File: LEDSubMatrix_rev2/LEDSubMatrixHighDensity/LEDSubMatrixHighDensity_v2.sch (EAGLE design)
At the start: 145 parts, among them IC1 TLC5955DCAR, IC2 TLC5955DCAR, IC3 TLC5955DCAR, IC4 TLC5955DCAR, IC5 TLC5955DCAR, IC6 TLC5955DCAR, IC7 TLC5955DCAR, IC8 TLC5955DCAR

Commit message: Updated pinouts to align with control board
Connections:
- new net 3V3_LOGIC: C1.1, C1B.1, C2.1, C2B.1, C3.1, C3B.1, C4.1, C4B.1, C5.1, C5B.1, C6.1, C6B.1, C7.1, C7B.1, C8.1, C8B.1, IC1.VCC, IC2.VCC, IC3.VCC, IC4.VCC, IC5.VCC, IC6.VCC, IC7.VCC, IC8.VCC, SV1.1
- net 3V3: no longer C1.1, C1B.1, C2.1, C2B.1, C3.1, C3B.1, C4.1, C4B.1, C5.1, C5B.1, C6.1, C6B.1, C7.1, C7B.1, C8.1, C8B.1, IC1.VCC, IC2.VCC, IC3.VCC, IC4.VCC, IC5.VCC, IC6.VCC, IC7.VCC, IC8.VCC
- net GND: now also SV1.2, SV1.4; no longer SV1.10, SV1.12, SV1.9
- net GSCLK: now also SV1.3; no longer SV1.11
- net SCLK: now also SV1.7; no longer SV1.1
- net SIN_1,2: now also SV1.12; no longer SV1.2
- net SIN_3,4: now also SV1.11; no longer SV1.3
- net SIN_5,6: now also SV1.10; no longer SV1.4
- net SIN_7,8: now also SV1.9; no longer SV1.7

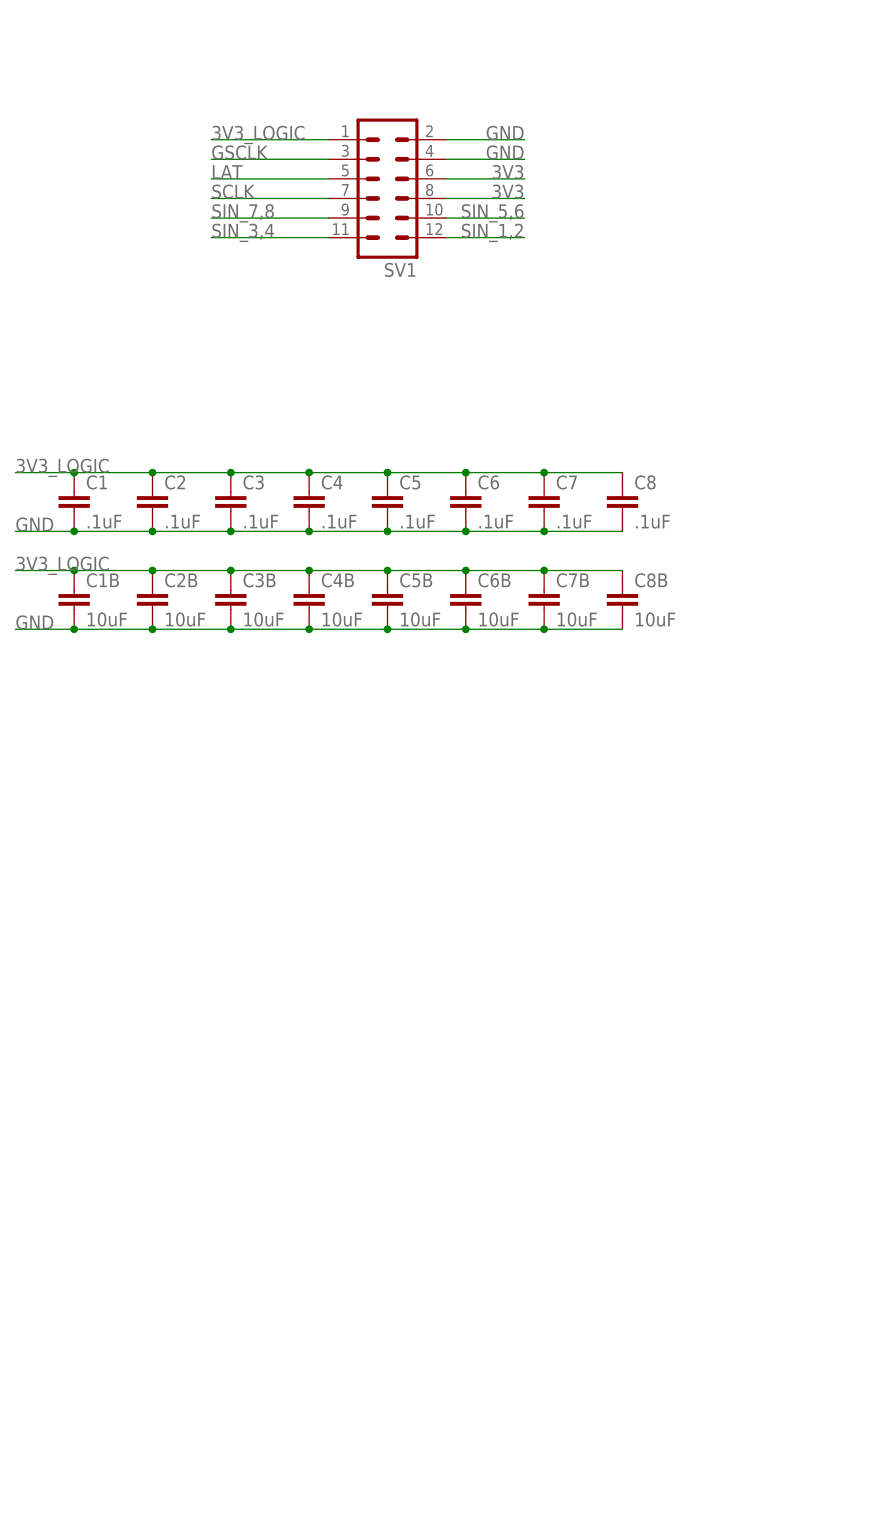
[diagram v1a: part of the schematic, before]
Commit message: Added logic buffers to LED matrix
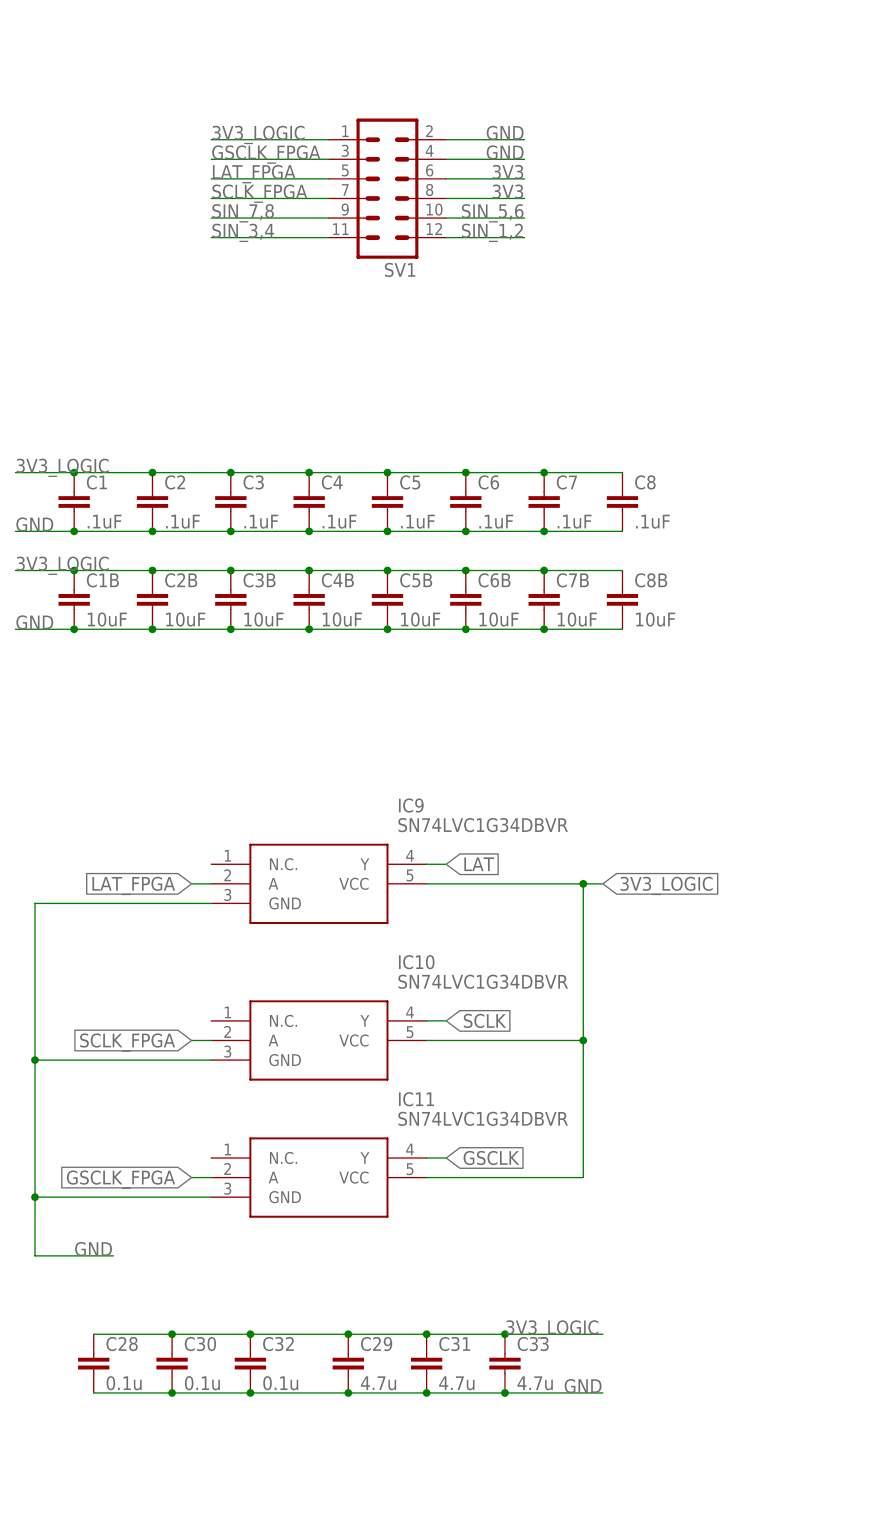
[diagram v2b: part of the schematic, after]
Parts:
- added C28, C30, C32: 0.1u, GTOR - Passive Components:CAP_SMDC0603
- added C29, C31, C33: 4.7u, GTOR - Passive Components:CAP_SMDC0603
- added IC10, IC11, IC9: SN74LVC1G34DBVR, SN74LVC1G34DBVR:SN74LVC1G34DBVR
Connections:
- new net GSCLK_FPGA: IC11.A, SV1.3
- new net LAT_FPGA: IC9.A, SV1.5
- new net SCLK_FPGA: IC10.A, SV1.7
- net 3V3_LOGIC: now also C28.1, C29.1, C30.1, C31.1, C32.1, C33.1, IC10.VCC, IC11.VCC, IC9.VCC
- net GND: now also C28.2, C29.2, C30.2, C31.2, C32.2, C33.2, IC10.GND, IC11.GND, IC9.GND
- net GSCLK: now also IC11.Y; no longer SV1.3
- net LAT: now also IC9.Y; no longer SV1.5
- net SCLK: now also IC10.Y; no longer SV1.7
